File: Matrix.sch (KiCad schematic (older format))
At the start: 114 parts

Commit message: Add in missing backspace stabs
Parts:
- K_BACK1: footprint MX_Alps_Hybrid:MX-1U-NoLED -> MX_Alps_Hybrid:MX-2U-NoLED
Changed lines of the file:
@@
 F 0 "K_BACK1" H 7800 1350 60  0000 C CNN
 F 1 "MX-2U" H 7800 1275 20  0000 C CNN
-F 2 "MX_Alps_Hybrid:MX-1U-NoLED" H 7775 1200 60  0001 C CNN
+F 2 "MX_Alps_Hybrid:MX-2U-NoLED" H 7775 1200 60  0001 C CNN
 F 3 "" H 7775 1200 60  0001 C CNN
 	1    7800 1225

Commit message: Update spacebar
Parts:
- removed SP2: MX-7U, MX_Alps_Hybrid:MX-7U-ReversedStabilizers-NoLED, symbol MX-1U
- SP1: value MX-6.25U -> MX-7U; footprint MX_Alps_Hybrid:MX-6.25U-ReversedStabilizers-NoLED -> MX_Alps_Hybrid:MX-7U-ReversedStabilizers-NoLED
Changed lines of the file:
@@
 P 4200 3725
 F 0 "SP1" H 4200 3850 60  0000 C CNN
-F 1 "MX-6.25U" H 4200 3775 20  0000 C CNN
-F 2 "MX_Alps_Hybrid:MX-6.25U-ReversedStabilizers-NoLED" H 4175 3700 60  0001 C CNN
+F 1 "MX-7U" H 4200 3775 20  0000 C CNN
+F 2 "MX_Alps_Hybrid:MX-7U-ReversedStabilizers-NoLED" H 4175 3700 60  0001 C CNN
 F 3 "" H 4175 3700 60  0001 C CNN
 	1    4200 3725
-	1    0    0    -1
-$EndComp
-$Comp
-L D_Small D55
-U 1 1 5A674270
-P 4100 4000
-F 0 "D55" H 4050 4080 50  0000 L CNN
-F 1 "D_Small" H 3950 3920 50  0000 L CNN
-F 2 "Diodes_SMD:D_SOD-123" V 4100 4000 50  0001 C CNN
-F 3 "" V 4100 4000 50  0001 C CNN
-	1    4100 4000
-	0    -1   -1   0
-$EndComp
-$Comp
-L MX-1U SP2
-U 1 1 5A67E802
-P 4200 4350
-F 0 "SP2" H 4200 4475 60  0000 C CNN
-F 1 "MX-7U" H 4200 4400 20  0000 C CNN
-F 2 "MX_Alps_Hybrid:MX-7U-ReversedStabilizers-NoLED" H 4175 4325 60  0001 C CNN
-F 3 "" H 4175 4325 60  0001 C CNN
-	1    4200 4350
 	1    0    0    -1
 $EndComp
@@
 	5975 3275 5900 3275
 Wire Wire Line
-	3975 3900 4175 3900
-Wire Wire Line
-	3975 4525 4175 4525
-Wire Wire Line
 	1675 1025 1675 3075
 Connection ~ 1675 2450
@@
 Connection ~ 1675 2575
 Wire Wire Line
-	4375 1025 4375 4325
+	4375 1025 4375 3700
 Connection ~ 4375 2450
 Connection ~ 4375 1825
@@
 Wire Wire Line
 	4675 4100 4100 4100
-Wire Wire Line
-	3975 3900 3975 4525
-Connection ~ 4100 3900
 Wire Wire Line
 	7975 2450 8425 2450
@@
 Wire Wire Line
 	7575 2450 7525 2450
+$Comp
+L D_Small D55
+U 1 1 5A674270
+P 4100 4000
+F 0 "D55" H 4050 4080 50  0000 L CNN
+F 1 "D_Small" H 3950 3920 50  0000 L CNN
+F 2 "Diodes_SMD:D_SOD-123" V 4100 4000 50  0001 C CNN
+F 3 "" V 4100 4000 50  0001 C CNN
+	1    4100 4000
+	0    -1   -1   0
+$EndComp
+Wire Wire Line
+	4100 3900 4175 3900
 $EndSCHEMATC

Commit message: Remove ISO
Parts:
- removed D45: D_Small, Diodes_SMD:D_SOD-123, symbol D_Small
- removed K_ENTER2: MX-ISO, MX_Alps_Hybrid:MX-ISO-Combined-ReversedStabilizers-NoLED, symbol MX-1U
- removed K_ISO\1, K_ISO`1: MX-1U, MX_Alps_Hybrid:MX-1U-NoLED, symbol MX-1U
- removed K_SHIFT2: MX-1.25U, MX_Alps_Hybrid:MX-1.25U-NoLED, symbol MX-1U
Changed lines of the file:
@@
-$EndComp
-$Comp
-L MX-1U K_ISO`1
-U 1 1 5A649875
-P 7350 2475
-F 0 "K_ISO`1" H 7350 2600 60  0000 C CNN
-F 1 "MX-1U" H 7350 2525 20  0000 C CNN
-F 2 "MX_Alps_Hybrid:MX-1U-NoLED" H 7325 2450 60  0001 C CNN
-F 3 "" H 7325 2450 60  0001 C CNN
-	1    7350 2475
-	1    0    0    -1
 $EndComp
 $Comp
@@
 $EndComp
 $Comp
-L MX-1U K_ISO\1
-U 1 1 5A64989C
-P 1950 3100
-F 0 "K_ISO\\1" H 1950 3225 60  0000 C CNN
-F 1 "MX-1U" H 1950 3150 20  0000 C CNN
-F 2 "MX_Alps_Hybrid:MX-1U-NoLED" H 1925 3075 60  0001 C CNN
-F 3 "" H 1925 3075 60  0001 C CNN
-	1    1950 3100
-	1    0    0    -1
-$EndComp
-$Comp
-L D_Small D45
-U 1 1 5A6498A2
-P 1850 3375
-F 0 "D45" H 1800 3455 50  0000 L CNN
-F 1 "D_Small" H 1700 3295 50  0000 L CNN
-F 2 "Diodes_SMD:D_SOD-123" V 1850 3375 50  0001 C CNN
-F 3 "" V 1850 3375 50  0001 C CNN
-	1    1850 3375
-	0    -1   -1   0
-$EndComp
-$Comp
 L MX-1U K_Z1
 U 1 1 5A6498A9
@@
 F 3 "" H 1025 2450 60  0001 C CNN
 	1    1050 2475
-	1    0    0    -1
-$EndComp
-$Comp
-L MX-1U K_ENTER2
-U 1 1 5A6653CE
-P 8250 2475
-F 0 "K_ENTER2" H 8250 2600 60  0000 C CNN
-F 1 "MX-ISO" H 8250 2525 20  0000 C CNN
-F 2 "MX_Alps_Hybrid:MX-ISO-Combined-ReversedStabilizers-NoLED" H 8225 2450 60  0001 C CNN
-F 3 "" H 8225 2450 60  0001 C CNN
-	1    8250 2475
-	1    0    0    -1
-$EndComp
-$Comp
-L MX-1U K_SHIFT2
-U 1 1 5A669FBA
-P 1050 3100
-F 0 "K_SHIFT2" H 1050 3225 60  0000 C CNN
-F 1 "MX-1.25U" H 1050 3150 20  0000 C CNN
-F 2 "MX_Alps_Hybrid:MX-1.25U-NoLED" H 1025 3075 60  0001 C CNN
-F 3 "" H 1025 3075 60  0001 C CNN
-	1    1050 3100
 	1    0    0    -1
 $EndComp
@@
 	7325 2025 7250 2025
 Wire Wire Line
-	7425 2025 7775 2025
-Wire Wire Line
 	1225 2650 1475 2650
 Wire Wire Line
@@
 Wire Wire Line
 	6875 2650 6800 2650
-Wire Wire Line
-	7700 2650 8225 2650
-Wire Wire Line
-	1025 3275 1475 3275
-Wire Wire Line
-	1925 3275 1850 3275
 Wire Wire Line
 	2375 3275 2300 3275
@@
 Connection ~ 1675 1825
 Connection ~ 1675 1200
-Wire Wire Line
-	2125 1025 2125 3075
 Connection ~ 2125 1200
 Wire Wire Line
@@
 Wire Wire Line
 	4675 4100 4100 4100
-Wire Wire Line
-	7975 2450 8425 2450
 Connection ~ 7775 2650
 Wire Wire Line
 	7975 1200 8425 1200
 Connection ~ 7775 1400
-Wire Wire Line
-	1675 3075 1225 3075
 Connection ~ 1400 3275
 Connection ~ 1525 1350
@@
 Connection ~ 3775 2600
 Connection ~ 4225 2600
-Connection ~ 1075 3225
 Connection ~ 1525 3225
-Connection ~ 1975 3225
 Connection ~ 2875 3225
 Connection ~ 2425 3225
@@
 Connection ~ 3775 3225
 Connection ~ 4225 3225
-Wire Wire Line
-	7425 2025 7425 2300
-Wire Wire Line
-	7425 2300 7325 2300
-Wire Wire Line
-	7325 2300 7325 2650
 Connection ~ 7700 2025
-Wire Wire Line
-	7975 1825 7575 1825
-Wire Wire Line
-	7575 1825 7575 2450
-Wire Wire Line
-	7575 2450 7525 2450
 $Comp
 L D_Small D55
@@
 Wire Wire Line
 	4100 3900 4175 3900
+Wire Wire Line
+	7775 2650 7700 2650
+Wire Wire Line
+	7700 2025 7775 2025
+Wire Wire Line
+	2125 1200 2125 1025
+Wire Wire Line
+	1475 3275 1400 3275
 $EndSCHEMATC

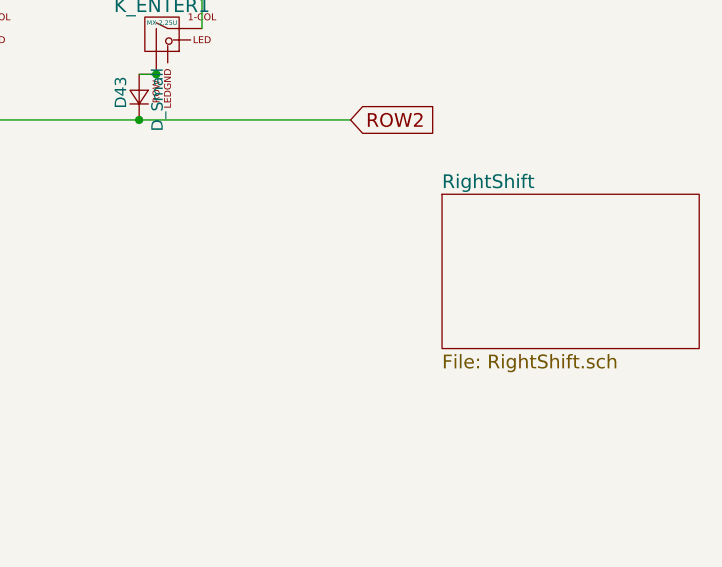
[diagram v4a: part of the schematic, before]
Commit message: Remove LEDs for removed switches on schematic
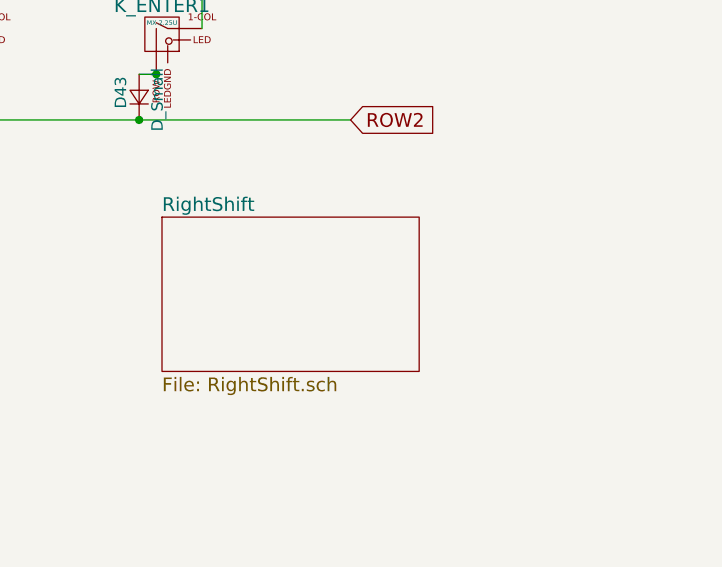
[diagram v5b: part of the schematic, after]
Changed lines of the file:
@@
 $EndComp
 $Sheet
-S 9025 3175 1125 675
+S 7800 3275 1125 675
 U 5A683C5B
 F0 "RightShift" 60

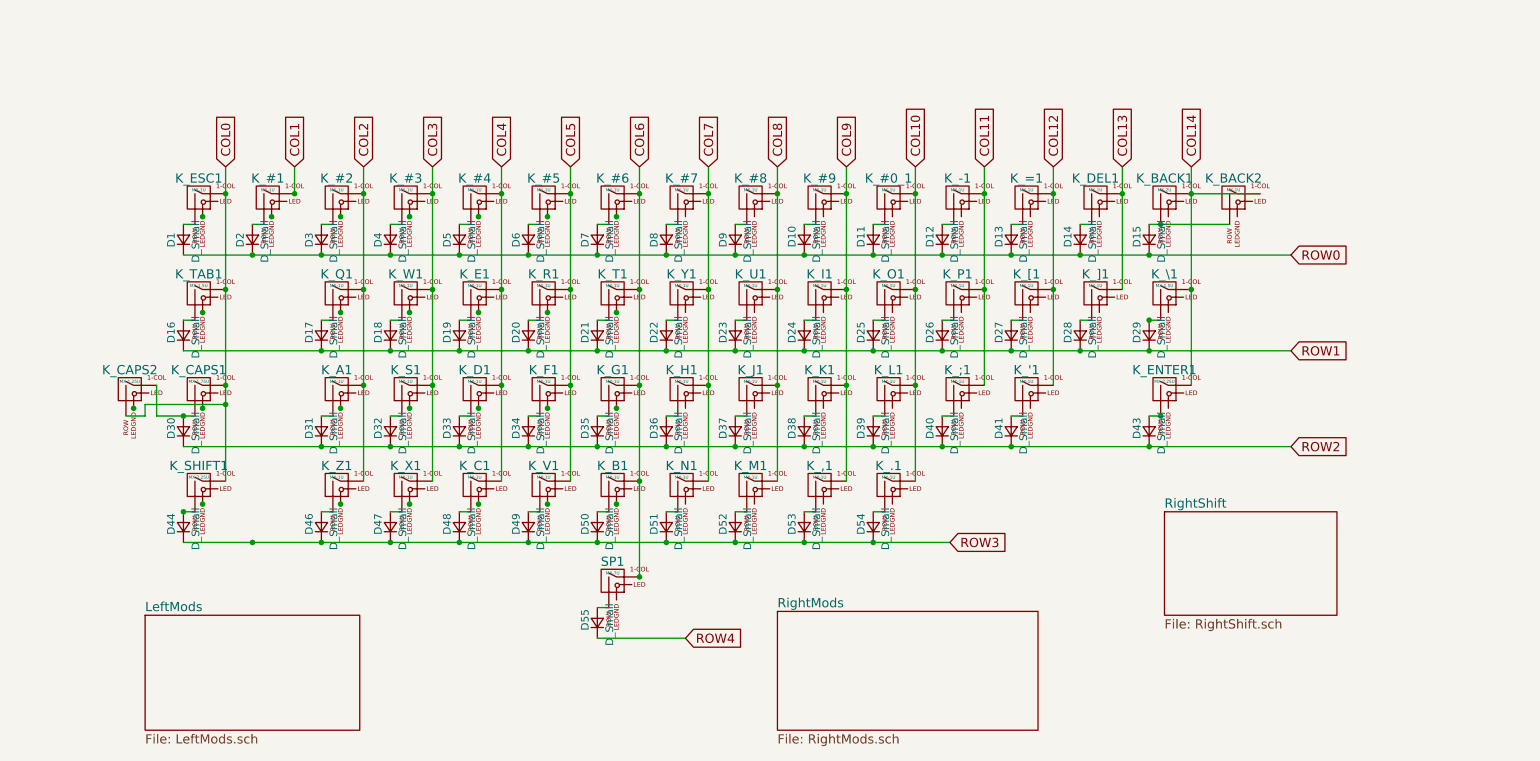
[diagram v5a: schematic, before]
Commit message: Revert LED structure
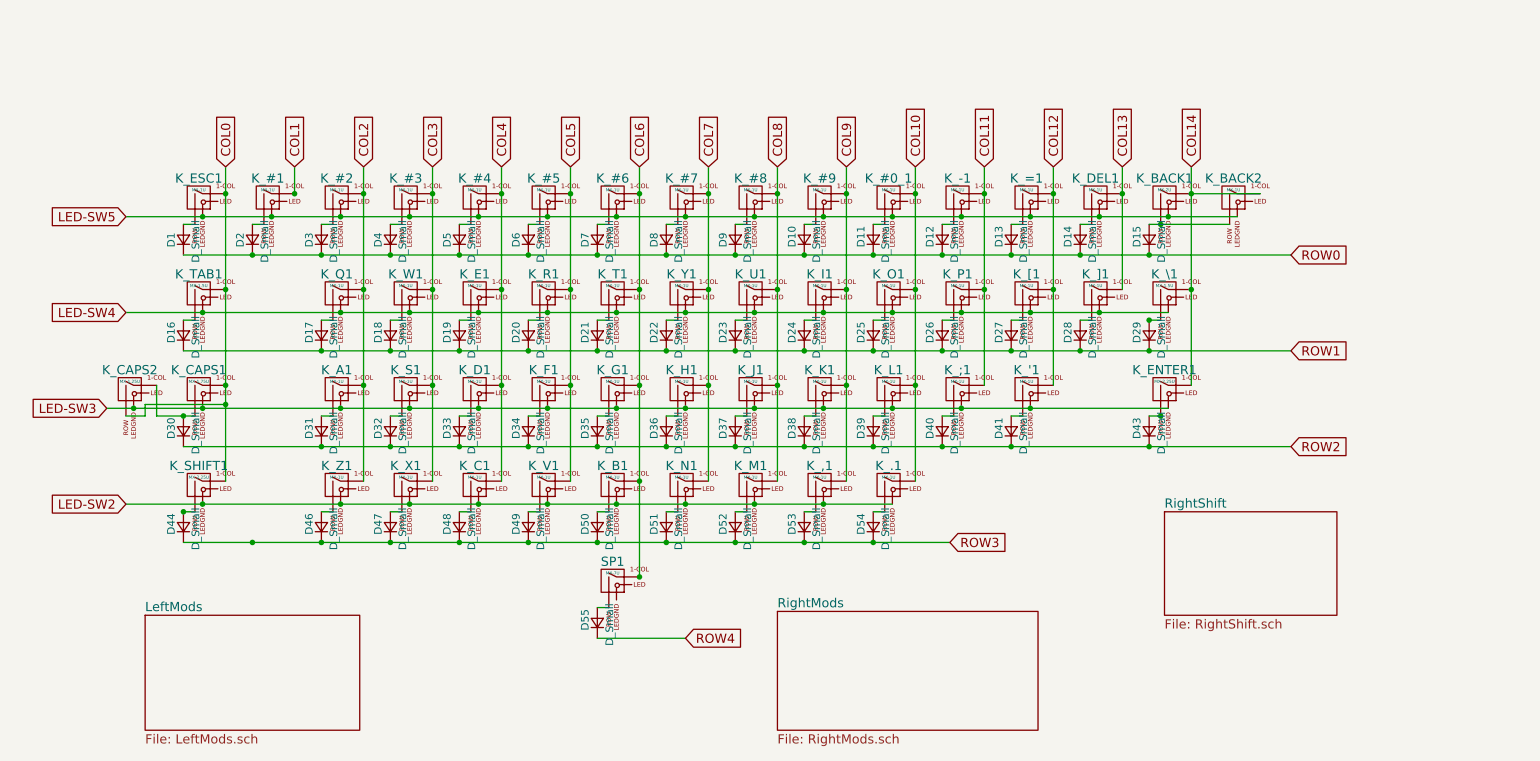
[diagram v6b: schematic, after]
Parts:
- K_#0_1, K_#1, K_#2, K_#3, K_#4, K_#5, K_#6, K_#7, K_#8, K_#9, K_'1, K_,1, K_-1, K_.1, K_;1, K_=1, K_A1, K_B1, K_BACK2, K_C1, K_D1, K_DEL1, K_E1, K_ESC1, K_F1, K_G1, K_H1, K_I1, K_J1, K_K1, K_L1, K_M1, K_N1, K_O1, K_P1, K_Q1, K_R1, K_S1, K_T1, K_U1, K_V1, K_W1, K_X1, K_Y1, K_Z1, K_[1, K_]1: footprint MX_Alps_Hybrid:MX-1U-NoLED -> MX_Alps_Hybrid:MX-1U
- K_BACK1: footprint MX_Alps_Hybrid:MX-2U-NoLED -> MX_Alps_Hybrid:MX-2U
- K_CAPS1: footprint MX_Alps_Hybrid:MX-1.75U-NoLED -> MX_Alps_Hybrid:MX-1.75U
- K_CAPS2: footprint MX_Alps_Hybrid:MX-1.25U-NoLED -> MX_Alps_Hybrid:MX-1.25U
- K_ENTER1, K_SHIFT1: footprint MX_Alps_Hybrid:MX-2.25U-NoLED -> MX_Alps_Hybrid:MX-2.25U
- K_TAB1, K_\1: footprint MX_Alps_Hybrid:MX-1.5U-NoLED -> MX_Alps_Hybrid:MX-1.5U
- SP1: footprint MX_Alps_Hybrid:MX-7U-ReversedStabilizers-NoLED -> MX_Alps_Hybrid:MX-7U-ReversedStabilizers
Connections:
- net LED-SW5: now reaches K_ESC1.4 (LEDGND)
- net LED-SW5: now also K_#0_1.4 (LEDGND), K_#1.4 (LEDGND), K_#2.4 (LEDGND), K_#3.4 (LEDGND), K_#4.4 (LEDGND), K_#5.4 (LEDGND), K_#6.4 (LEDGND), K_#7.4 (LEDGND), K_#8.4 (LEDGND), K_#9.4 (LEDGND), K_-1.4 (LEDGND), K_=1.4 (LEDGND), K_BACK1.4 (LEDGND), K_BACK2.4 (LEDGND), K_DEL1.4 (LEDGND)
- net LED-SW4: now reaches K_TAB1.4 (LEDGND)
- net LED-SW4: now also K_E1.4 (LEDGND), K_I1.4 (LEDGND), K_O1.4 (LEDGND), K_P1.4 (LEDGND), K_Q1.4 (LEDGND), K_R1.4 (LEDGND), K_T1.4 (LEDGND), K_U1.4 (LEDGND), K_W1.4 (LEDGND), K_Y1.4 (LEDGND), K_[1.4 (LEDGND), K_\1.4 (LEDGND), K_]1.4 (LEDGND)
- net LED-SW3: now reaches K_CAPS1.4 (LEDGND)
- net LED-SW3: now also K_'1.4 (LEDGND), K_;1.4 (LEDGND), K_A1.4 (LEDGND), K_CAPS2.4 (LEDGND), K_D1.4 (LEDGND), K_ENTER1.4 (LEDGND), K_F1.4 (LEDGND), K_G1.4 (LEDGND), K_H1.4 (LEDGND), K_J1.4 (LEDGND), K_K1.4 (LEDGND), K_L1.4 (LEDGND), K_S1.4 (LEDGND)
- net LED-SW2: now reaches K_SHIFT1.4 (LEDGND)
- net LED-SW2: now also K_,1.4 (LEDGND), K_.1.4 (LEDGND), K_B1.4 (LEDGND), K_C1.4 (LEDGND), K_M1.4 (LEDGND), K_N1.4 (LEDGND), K_V1.4 (LEDGND), K_X1.4 (LEDGND), K_Z1.4 (LEDGND)

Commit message: Begin routing
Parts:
- K_CAPS2: footprint MX_Alps_Hybrid:MX-1.25U -> MX_Alps_Hybrid:MX-1.25U-FLIPPED
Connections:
- net LED-CS1: now reaches K_ESC1.3 (LED)
- net LED-CS1: now also K_CAPS1.3 (LED), K_CAPS2.3 (LED), K_SHIFT1.3 (LED), K_TAB1.3 (LED)
- net LED-CS12: now reaches K_-1.3 (LED)
- net LED-CS12: now also K_;1.3 (LED), K_P1.3 (LED)
- net LED-CS2: now reaches K_#1.3 (LED)
- net LED-CS3: now reaches K_#2.3 (LED)
- net LED-CS3: now also K_A1.3 (LED), K_Q1.3 (LED), K_Z1.3 (LED)
- net LED-CS4: now reaches K_#3.3 (LED)
- net LED-CS4: now also K_S1.3 (LED), K_W1.3 (LED), K_X1.3 (LED)
- net LED-CS5: now reaches K_#4.3 (LED)
- net LED-CS5: now also K_C1.3 (LED), K_D1.3 (LED), K_E1.3 (LED)
- net LED-CS6: now reaches K_#5.3 (LED)
- net LED-CS6: now also K_F1.3 (LED), K_R1.3 (LED), K_V1.3 (LED)
- net LED-CS7: now reaches K_#6.3 (LED)
- net LED-CS7: now also K_B1.3 (LED), K_G1.3 (LED), K_T1.3 (LED)
- net LED-CS8: now reaches K_#7.3 (LED)
- net LED-CS8: now also K_H1.3 (LED), K_N1.3 (LED), K_Y1.3 (LED)
- net LED-CS9: now reaches K_#8.3 (LED)
- net LED-CS9: now also K_J1.3 (LED), K_M1.3 (LED), K_U1.3 (LED)
- net LED-CS10: now reaches K_#9.3 (LED)
- net LED-CS10: now also K_,1.3 (LED), K_I1.3 (LED), K_K1.3 (LED)
- net LED-CS11: now reaches K_#0_1.3 (LED)
- net LED-CS11: now also K_.1.3 (LED), K_L1.3 (LED), K_O1.3 (LED)
- net LED-CS13: now reaches K_=1.3 (LED)
- net LED-CS13: now also K_'1.3 (LED), K_[1.3 (LED)
- net LED-CS14: now reaches K_DEL1.3 (LED)
- net LED-CS14: now also K_]1.3 (LED)
- net LED-CS15: now reaches K_BACK1.3 (LED)
- net LED-CS15: now also K_BACK2.3 (LED), K_ENTER1.3 (LED), K_\1.3 (LED)
- net LED-SW1: now reaches SP1.4 (LEDGND)
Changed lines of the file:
@@
 F 0 "K_CAPS2" H 1050 2600 60  0000 C CNN
 F 1 "MX-1.25U" H 1050 2525 20  0000 C CNN
-F 2 "MX_Alps_Hybrid:MX-1.25U" H 1025 2450 60  0001 C CNN
+F 2 "MX_Alps_Hybrid:MX-1.25U-FLIPPED" H 1025 2450 60  0001 C CNN
 F 3 "" H 1025 2450 60  0001 C CNN
 	1    1050 2475
@@
 Connection ~ 5125 3225
 Connection ~ 5575 3225
+Wire Wire Line
+	1625 675  1625 3125
+Connection ~ 1625 1875
+Wire Wire Line
+	1625 2500 1175 2500
+Connection ~ 1625 2500
+Connection ~ 1625 1250
+Text GLabel 1625 675  1    60   Input ~ 0
+LED-CS1
+Wire Wire Line
+	2525 675  2525 3125
+Connection ~ 2525 2500
+Connection ~ 2525 1875
+Connection ~ 2525 1250
+Text GLabel 2525 675  1    60   Input ~ 0
+LED-CS3
+Wire Wire Line
+	2075 1250 2075 675
+Text GLabel 2075 675  1    60   Input ~ 0
+LED-CS2
+Wire Wire Line
+	2975 675  2975 3125
+Connection ~ 2975 2500
+Connection ~ 2975 1875
+Connection ~ 2975 1250
+Text GLabel 2975 675  1    60   Input ~ 0
+LED-CS4
+Wire Wire Line
+	3425 675  3425 3125
+Connection ~ 3425 2500
+Connection ~ 3425 1875
+Connection ~ 3425 1250
+Text GLabel 3425 675  1    60   Input ~ 0
+LED-CS5
+Wire Wire Line
+	3875 675  3875 3125
+Connection ~ 3875 2500
+Connection ~ 3875 1875
+Connection ~ 3875 1250
+Text GLabel 3875 675  1    60   Input ~ 0
+LED-CS6
+Wire Wire Line
+	4225 3850 3450 3850
+Text GLabel 3450 3850 0    60   Input ~ 0
+LED-SW1
+Wire Wire Line
+	4325 675  4325 3125
+Connection ~ 4325 2500
+Connection ~ 4325 1875
+Connection ~ 4325 1250
+Text GLabel 4325 675  1    60   Input ~ 0
+LED-CS7
+Wire Wire Line
+	4775 675  4775 3125
+Connection ~ 4775 2500
+Connection ~ 4775 1875
+Connection ~ 4775 1250
+Text GLabel 4775 675  1    60   Input ~ 0
+LED-CS8
+Wire Wire Line
+	5225 675  5225 3125
+Connection ~ 5225 2500
+Connection ~ 5225 1875
+Connection ~ 5225 1250
+Text GLabel 5225 675  1    60   Input ~ 0
+LED-CS9
+Wire Wire Line
+	5675 675  5675 3125
+Connection ~ 5675 2500
+Connection ~ 5675 1875
+Connection ~ 5675 1250
+Text GLabel 5675 675  1    60   Input ~ 0
+LED-CS10
+Wire Wire Line
+	6125 675  6125 3125
+Connection ~ 6125 2500
+Connection ~ 6125 1875
+Connection ~ 6125 1250
+Text GLabel 6125 675  1    60   Input ~ 0
+LED-CS11
+Wire Wire Line
+	6575 675  6575 2500
+Connection ~ 6575 1875
+Connection ~ 6575 1250
+Text GLabel 6575 675  1    60   Input ~ 0
+LED-CS12
+Wire Wire Line
+	7025 675  7025 2500
+Connection ~ 7025 1875
+Connection ~ 7025 1250
+Text GLabel 7025 675  1    60   Input ~ 0
+LED-CS13
+Wire Wire Line
+	7475 675  7475 1875
+Connection ~ 7475 1250
+Text GLabel 7475 675  1    60   Input ~ 0
+LED-CS14
+Wire Wire Line
+	7925 675  7925 2500
+Connection ~ 7925 1875
+Wire Wire Line
+	7925 1250 8375 1250
+Connection ~ 7925 1250
+Text GLabel 7925 675  1    60   Input ~ 0
+LED-CS15
 $EndSCHEMATC

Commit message: Fix spacebar LED
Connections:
- net LED-CS7: now also SP1.3 (LED)
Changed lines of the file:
@@
 LED-SW1
 Wire Wire Line
-	4325 675  4325 3125
+	4325 675  4325 3750
 Connection ~ 4325 2500
 Connection ~ 4325 1875
@@
 Text GLabel 7925 675  1    60   Input ~ 0
 LED-CS15
+Connection ~ 4325 3125
 $EndSCHEMATC
